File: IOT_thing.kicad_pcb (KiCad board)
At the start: 2 copper layers, 100 x 100 mm, 64 parts, among them J1 USB_C_Receptacle_USB2.0_16P, J2 Conn_01x04, J3 Screw_Terminal_01x03, J4 Screw_Terminal_01x08, J5 Screw_Terminal_01x02, J6 Conn_02x05_Odd_Even, K1 RT314A05, Q1 UMH3N, Q2 UMH3N, Q3 BC817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

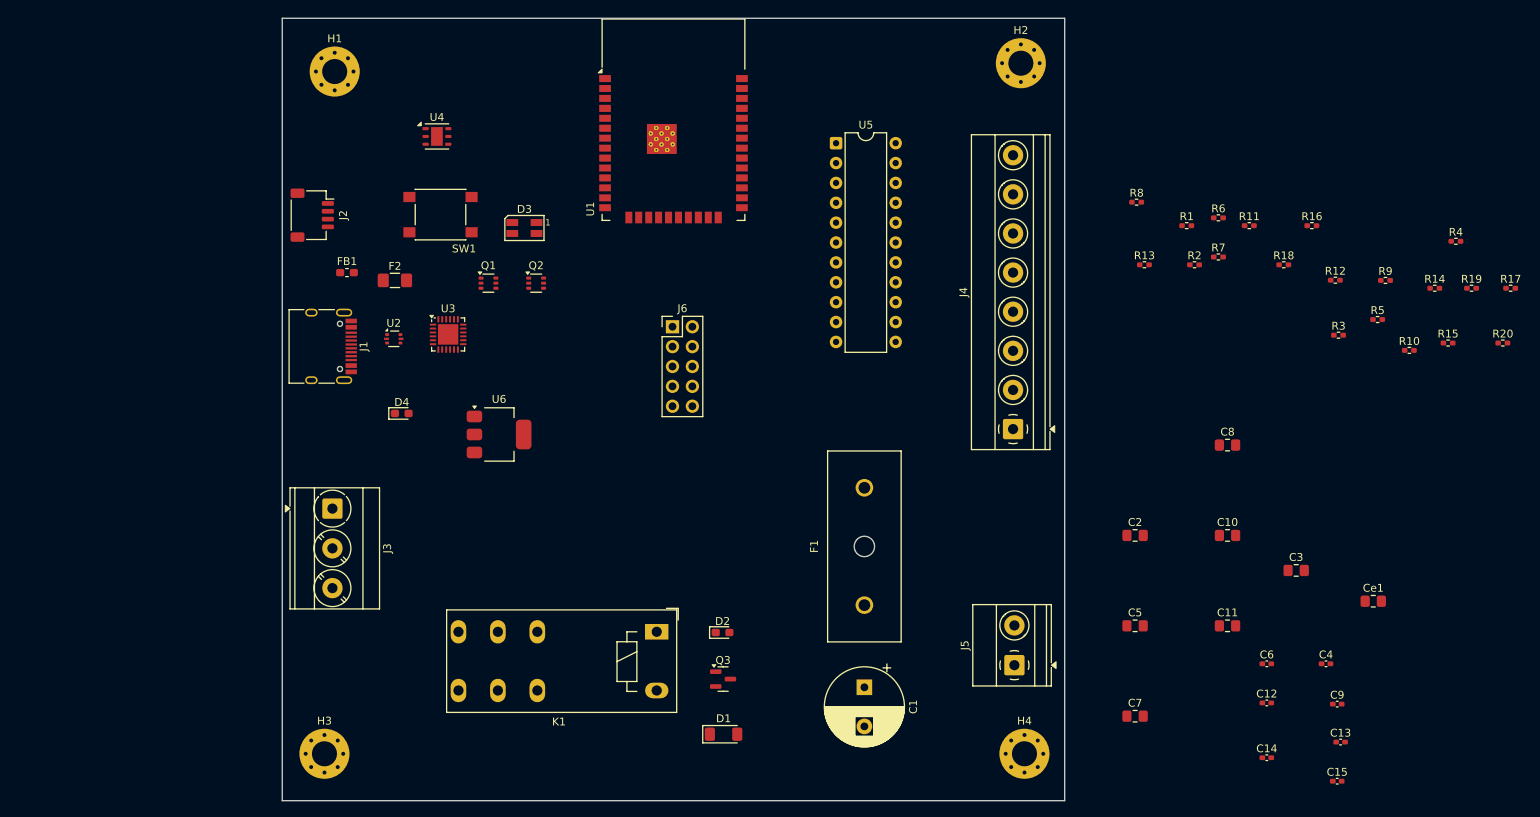
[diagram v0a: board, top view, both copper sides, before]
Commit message: Finished arranging the components
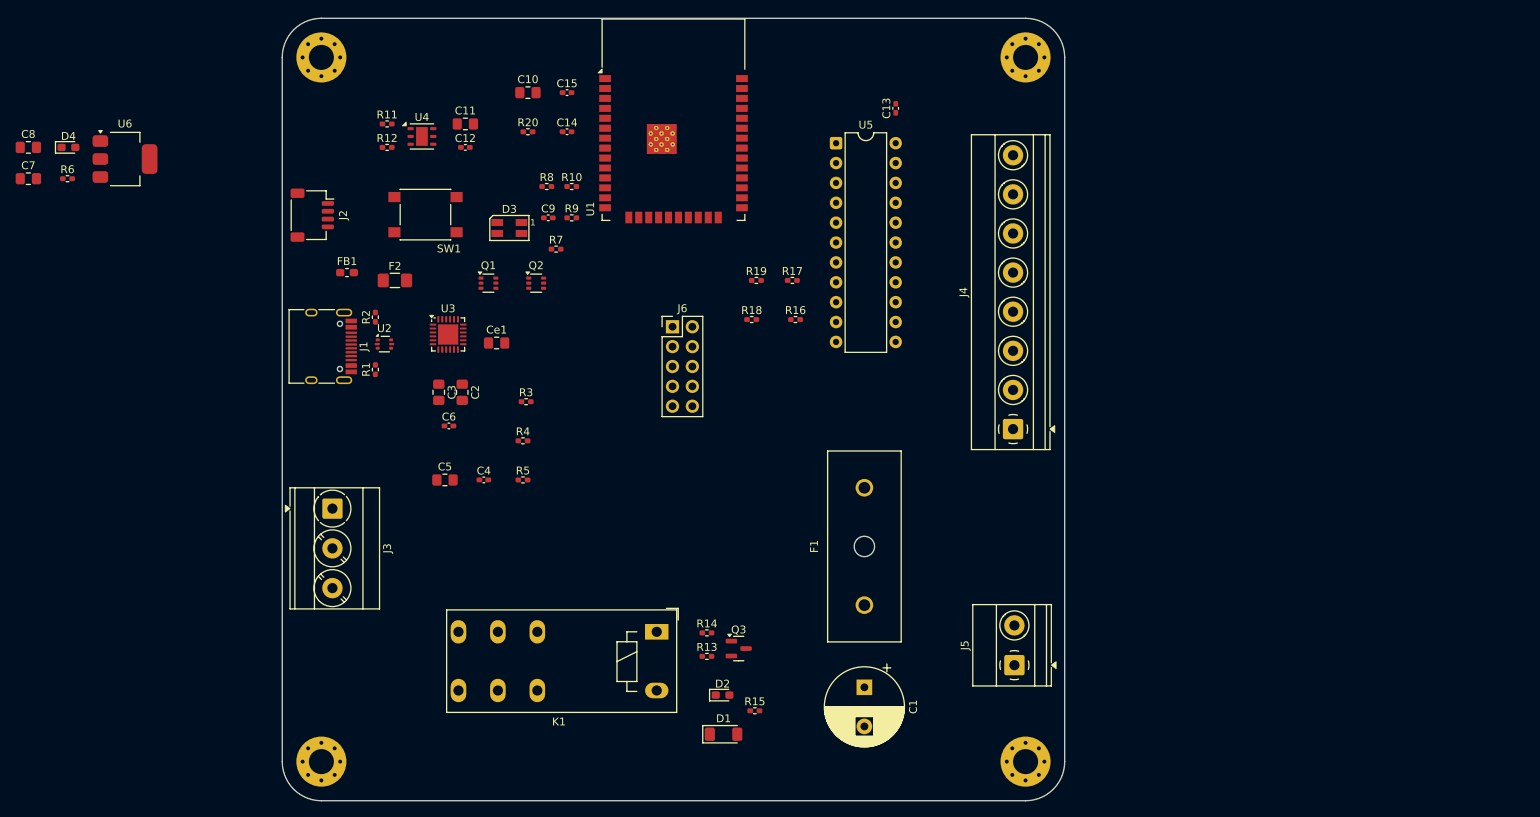
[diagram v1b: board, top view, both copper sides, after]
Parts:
- R20: value 1K -> 10K
- moved C8 157.9 mm to (26.1, 64.0)
- moved C7 157.2 mm to (26.1, 68.0)
- moved R6 147.2 mm to (31.1, 68.0)
- moved C15 132.0 mm to (95.0, 57.0)
- moved R20 127.5 mm to (90.0, 62.0)
- moved C12 124.6 mm to (82.0, 64.0)
- moved R12 122.4 mm to (72.0, 64.0)
- moved R4 121.9 mm to (89.4, 101.5)
- moved C14 120.0 mm to (95.0, 62.0)
- moved C9 118.4 mm to (92.6, 73.0)
- moved Ce1 116.8 mm to (86.0, 89.0)
- moved C11 116.6 mm to (82.0, 61.0)
- moved C3 111.9 mm to (78.6, 95.3), turned to -90 degrees
- moved R5 111.1 mm to (89.4, 106.5)
- moved R11 111.0 mm to (72.0, 61.0)
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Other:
- outline, holes or cut-outs redrawn
- copper layers 2 -> 4

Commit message: Arranged the layout and finalised the silkscreen
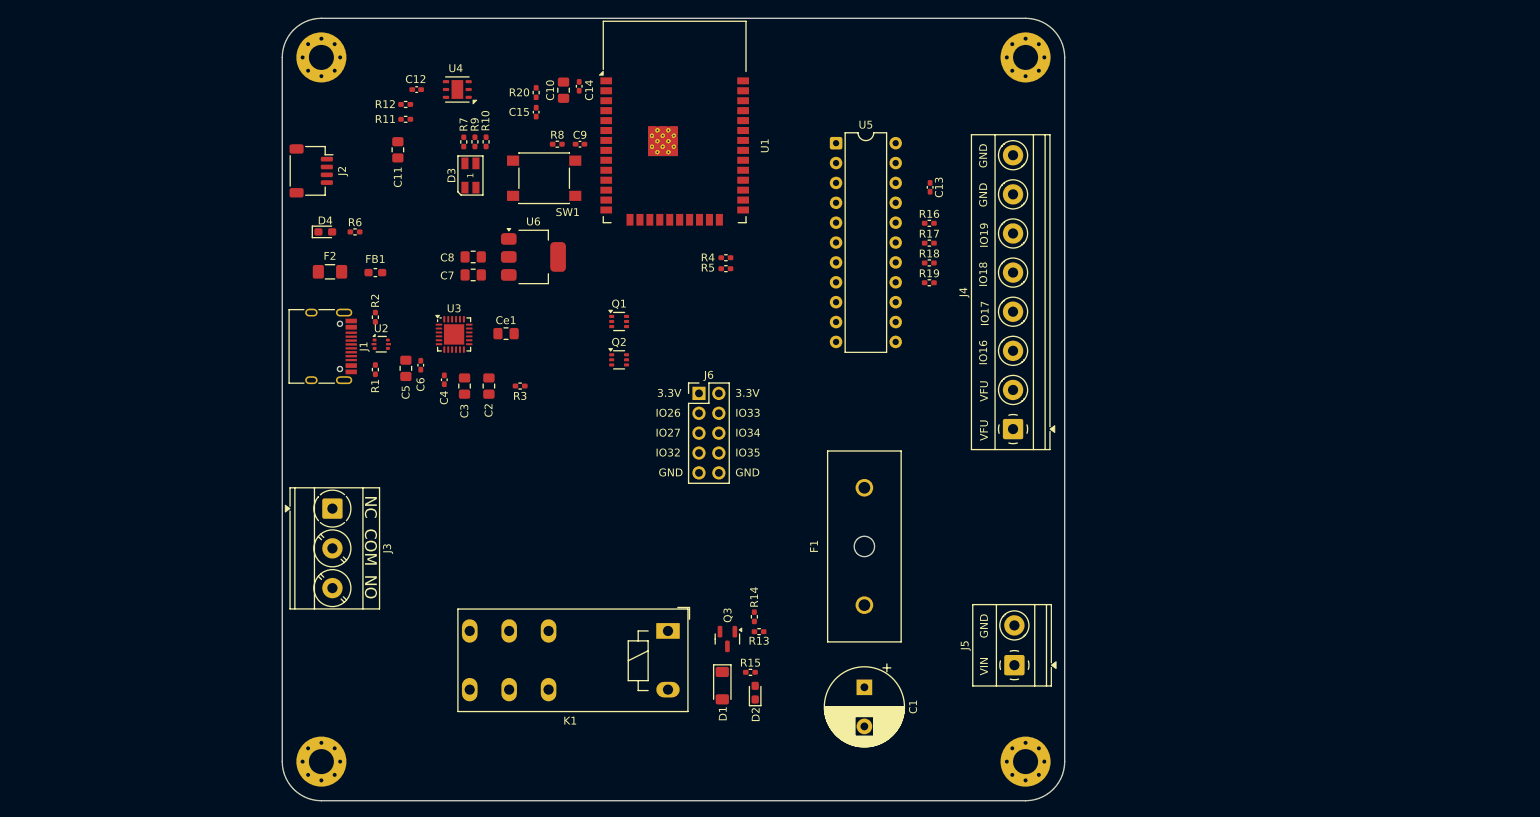
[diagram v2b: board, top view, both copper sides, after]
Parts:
- moved C8 58.5 mm to (83.0, 78.0), turned to 180 degrees
- moved C7 58.2 mm to (83.0, 80.3), turned to 180 degrees
- moved U6 53.7 mm to (90.7, 78.0)
- moved R5 37.4 mm to (115.3, 79.5)
- moved R6 37.4 mm to (67.9, 74.8), turned to 180 degrees
- moved R4 34.9 mm to (115.3, 78.1)
- moved D4 34.6 mm to (64.1, 74.8)
- moved R18 23.8 mm to (141.3, 78.8)
- moved R19 22.1 mm to (141.3, 81.3)
- moved R16 21.1 mm to (141.3, 73.7)
- moved R17 18.1 mm to (141.3, 76.2)
- moved R7 18.1 mm to (81.8, 63.3), turned to -90 degrees
- moved Q1 17.4 mm to (101.7, 86.2)
- moved SW1 15.9 mm to (92.1, 67.9)
- moved R9 15.7 mm to (83.2, 63.3), turned to -90 degrees
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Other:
- board text added: "3.3V"
- board text added: "COM"
- board text added: "GND"
- board text added: "IO16"
- board text added: "IO17"
- board text added: "IO18"
- board text added: "IO19"
- board text added: "IO26"
- board text added: "IO27"
- board text added: "IO32"
- board text added: "IO33"
- board text added: "IO34"
- board text added: "IO35"
- board text added: "NC"
- board text added: "NO"
- board text added: "VFU"
- board text added: "VIN"

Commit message: Finalised the project
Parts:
- U2: footprint Package_TO_SOT_SMD:SOT-666 -> iot-thing_Library_11:SOT-666
- U5: footprint Package_DIP:DIP-22_W7.62mm -> iot-thing_Library_11:DIP-20_W7.62mm
- moved C5 51.4 mm to (125.7, 96.2)
- moved C6 51.4 mm to (127.6, 95.7)
- moved H3 51.3 mm to (114.2, 134.0)
- moved R15 51.2 mm to (169.4, 125.4)
- moved R14 51.2 mm to (169.9, 118.3)
- moved D2 51.2 mm to (170.0, 128.1)
- moved Q3 51.2 mm to (166.4, 121.2)
- moved R13 51.2 mm to (170.5, 120.2)
- moved D1 51.2 mm to (165.8, 127.2)
- moved K1 51.2 mm to (158.8, 120.2)
- moved J2 50.9 mm to (113.1, 70.4)
- moved R7 50.8 mm to (132.5, 66.7)
- moved Q1 50.8 mm to (152.3, 90.8)
- moved Q2 50.8 mm to (152.3, 95.7)
- moved R9 50.8 mm to (133.9, 66.7)
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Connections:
- C15 pad 1: Net-(C15-Pad1) -> /EN
- H3 pad 1: GND -> unconnected-(H3-Pad1)_4
- Q2 pad 1: +3.3V -> /EN
- Q2 pad 4: +3.3V -> /EN
- R20 pad 2: Net-(C15-Pad1) -> /EN
- U1 pad 3: +3.3V -> /EN
- U1 pad 34: /TX -> /RX
- U1 pad 35: /RX -> /TX
- U2 pad 1: Net-(U3-D-) -> Net-(J1-D+-PadA6)
- U2 pad 4: Net-(J1-D+-PadA6) -> Net-(U3-D-)
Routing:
- net +5V: track 0.00 -> 211.0 mm, vias 0 -> 5
- net +3.3V: track 0.00 -> 155.0 mm, vias 0 -> 9
- net /EN: track 0.00 -> 72.4 mm, vias 0 -> 2
- net /SCL: track 0.00 -> 72.4 mm, vias 0 -> 4
- net /SDA: track 0.00 -> 70.4 mm, vias 0 -> 3
- net /RELAY: track 0.00 -> 61.3 mm
- net /GPIO35: track 0.00 -> 53.5 mm, vias 0 -> 2
- net GND: track 0.00 -> 52.9 mm, vias 0 -> 31
- net /GPIO34: track 0.00 -> 49.9 mm, vias 0 -> 2
- net /GPIO32: track 0.00 -> 45.0 mm, vias 0 -> 2
- net Net-(J3-Pin_1): track 0.00 -> 43.4 mm
- net /GPIO33: track 0.00 -> 41.7 mm, vias 0 -> 2
- net /SW: track 0.00 -> 39.7 mm, vias 0 -> 2
- net /LED_G: track 0.00 -> 39.6 mm, vias 0 -> 2
- net /GPIO27: track 0.00 -> 39.0 mm, vias 0 -> 2
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- added copper zone on B.Cu, net GND
- added copper zone on F.Cu, net GND
- added copper zone on In1.Cu, net GND
- added copper zone on In2.Cu, net GND
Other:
- board size 100 x 100 mm -> 95 x 88.1 mm
